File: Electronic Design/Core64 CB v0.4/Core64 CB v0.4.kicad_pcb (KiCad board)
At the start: 2 copper layers, 85 x 85 mm, 36 parts, among them J1 TSM-116-03-T-SV‎, J2 TSM-116-03-T-SV‎, U10 TS3A4751PWR, U11 TS3A4751PWR, U5 SI7210-B-01, U6 SI7210-B-02, U7 SI7210-B-03, U8 SI7210-B-04, U9 LTR-329ALS-01, X1 SFH11-NBPC-D03-ST-BK

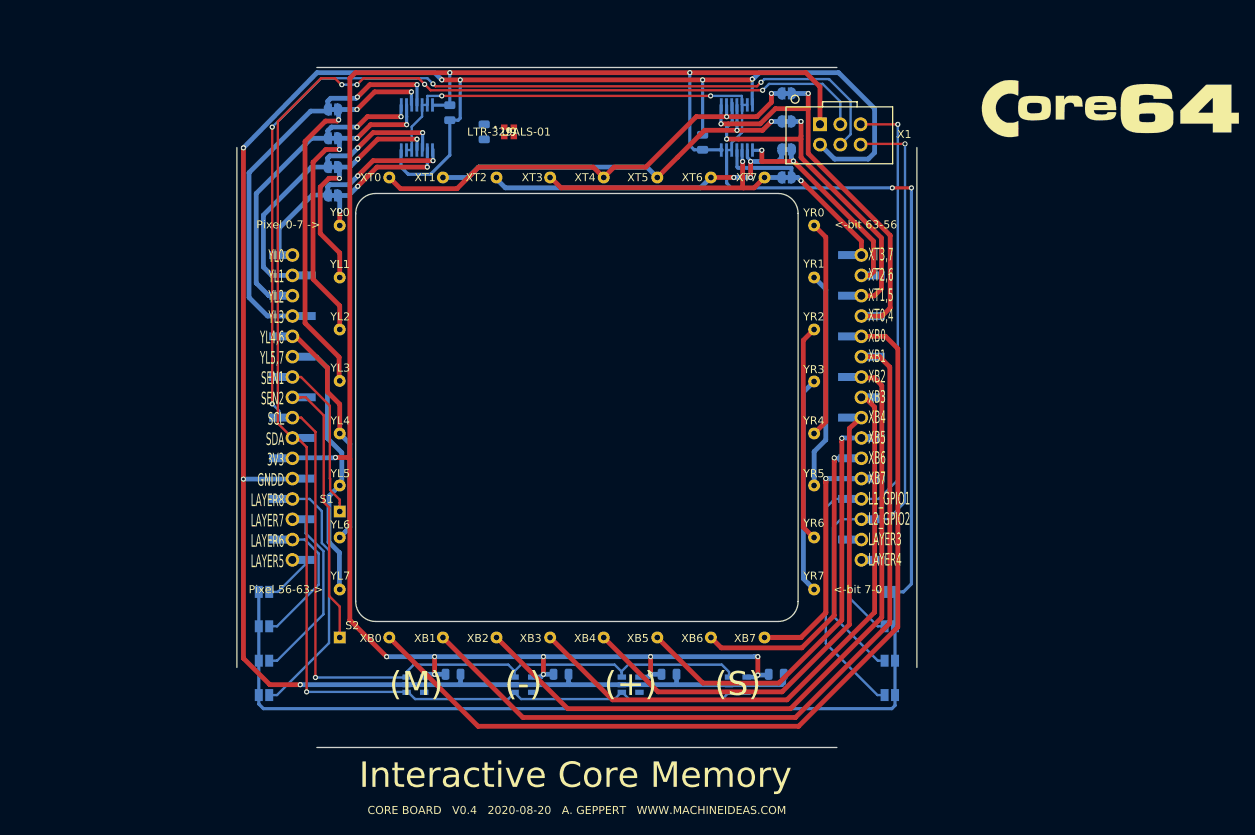
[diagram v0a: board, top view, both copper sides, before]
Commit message: Complete draft of Core Board with updated Core64 Logo
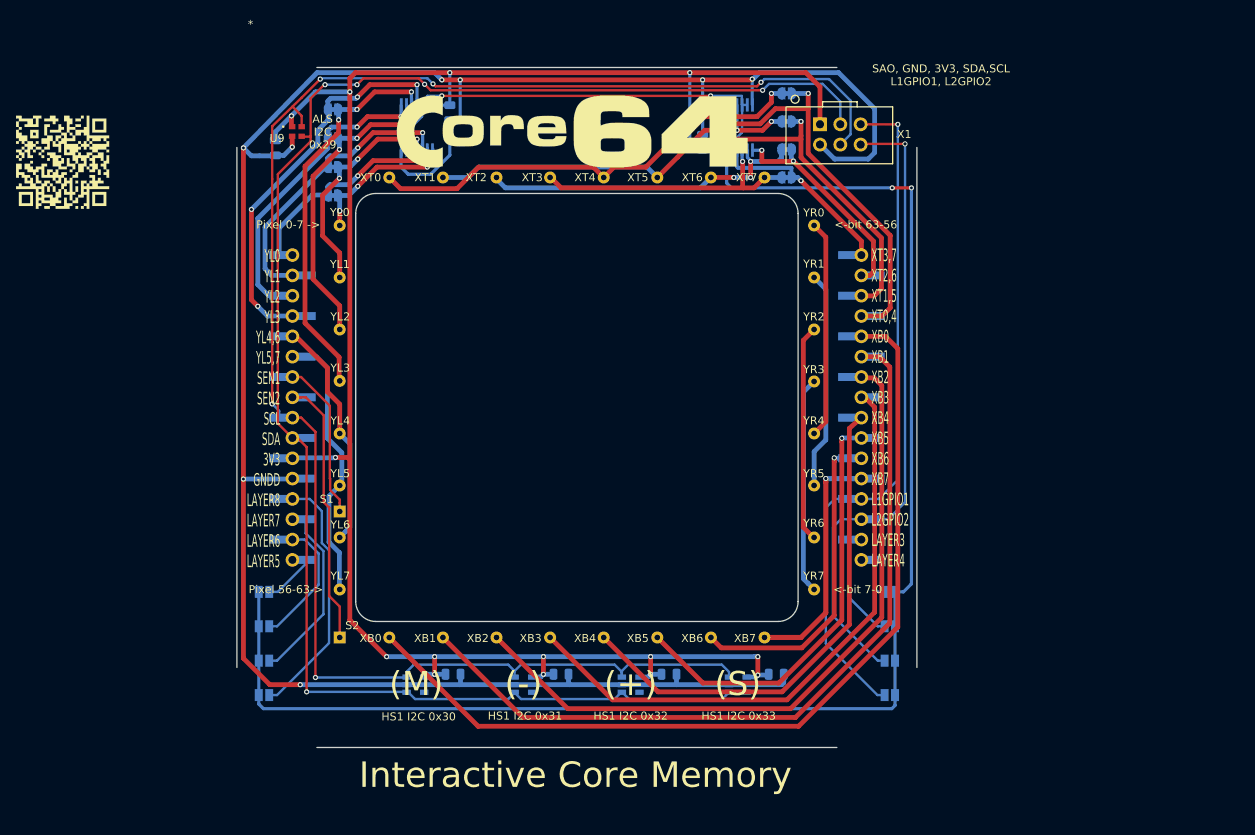
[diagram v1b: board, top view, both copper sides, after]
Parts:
- removed the L2 at (66.9, -37.0)
- added L1: Core_64_Logo_9mm_tall, Core_Memory_8x8_Array:Core64_Logo_9mm_tall, F.Cu at (0.00, -34.5)
- L2: renamed from L1; moved to F.Cu
- moved U9 26.5 mm to (-35.0, -34.5)
- moved C13 26.2 mm to (-37.7, -32.5)
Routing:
- net 3V3_800mA: track 233.9 -> 247.7 mm, vias 12 -> 14
- net GNDD: track 274.7 -> 283.0 mm, vias 7 -> 8
- net I2C_CLOCK: track 212.7 -> 215.7 mm
- net H_YL3: track 52.6 -> 51.1 mm, vias 2 -> 4
- net H_YL2: track 40.4 -> 39.1 mm
- net H_YL1: track 39.4 -> 38.2 mm
- net YL1: track 29.6 -> 28.6 mm
- net YL2: track 39.5 -> 38.5 mm
- net YL3: track 49.9 -> 49.0 mm
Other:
- board text added: "ALS I2C 0x29"
- board text added: "HS1 I2C 0x30"
- board text added: "HS1 I2C 0x31"
- board text added: "HS1 I2C 0x32"
- board text added: "HS1 I2C 0x33"
- board text added: "SAO, GND, 3V3, SDA,SCL L1GPIO1, L2GPIO2"
- board text added: "XT3,7 XT2,6 XT1,5 XT0,4 XB0 XB1 XB2 XB3 XB4 XB5 XB6 XB7 L1GPIO1 L2GPIO2 LAYER3 LAYER4"
- board text removed: "XT3,7 XT2,6 XT1,5 XT0,4 XB0 XB1 XB2 XB3 XB4 XB5 XB6 XB7 L1_GPIO1 L2_GPIO2 LAYER3 LAYER4"

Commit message: Update Core 64 logo
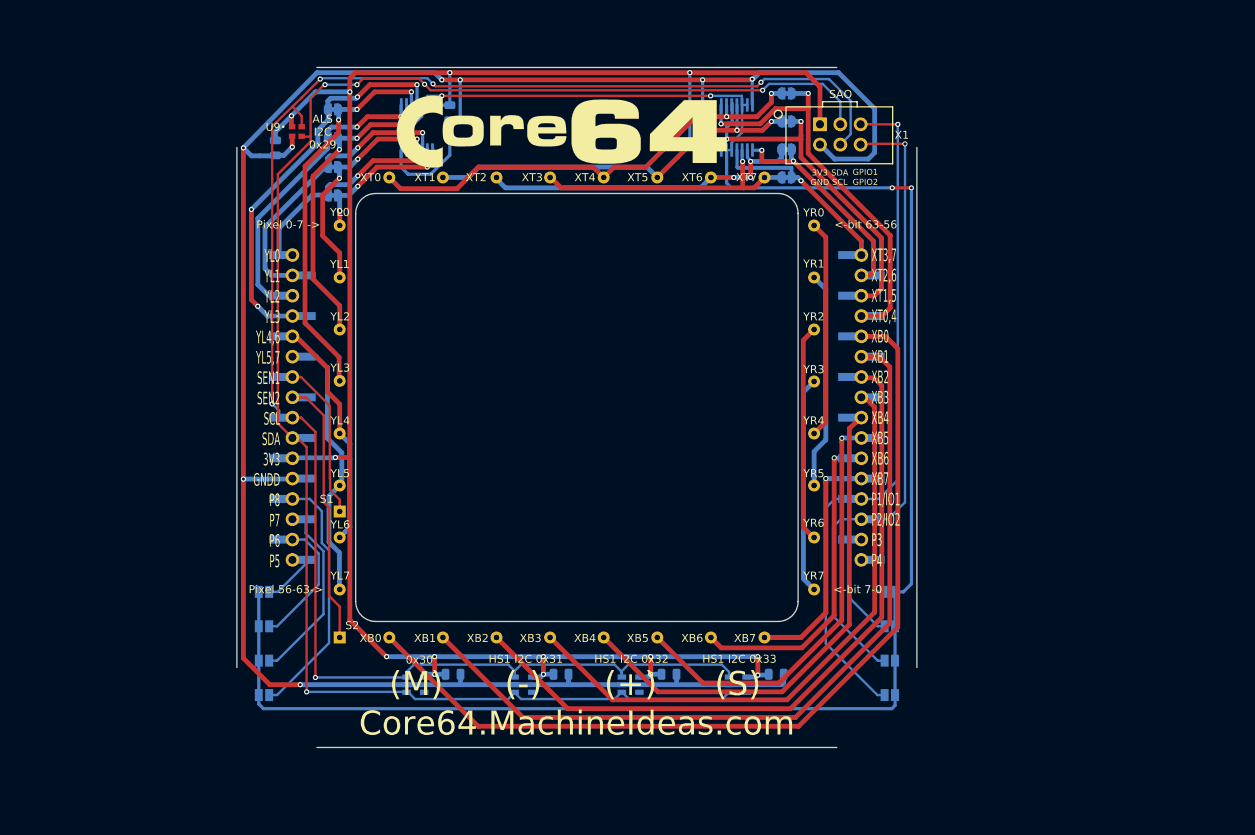
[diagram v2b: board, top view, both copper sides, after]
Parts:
- removed L2: Core_64_Github_Link, Core_Memory_8x8_Array:Github_Link
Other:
- board text added: "0x30"
- board text added: "CORE BOARD V0.4 2020-08-21 ANDY GEPPERT CORE64.MACHINEIDEAS.COM"
- board text added: "Core64.MachineIdeas.com"
- board text added: "XT3,7 XT2,6 XT1,5 XT0,4 XB0 XB1 XB2 XB3 XB4 XB5 XB6 XB7 P1/IO1 P2/IO2 P3 P4"
- board text added: "YL0 YL1 YL2 YL3 YL4,6 YL5,7 SEN1 SEN2 SCL SDA 3V3 GNDD P8 P7 P6 P5"
- board text removed: "CORE BOARD V0.3 2020-04-17 A. GEPPERT WWW.MACHINEIDEAS.COM"
- board text removed: "CORE BOARD V0.4 2020-08-20 A. GEPPERT WWW.MACHINEIDEAS.COM"
- board text removed: "HS1 I2C 0x30"
- board text removed: "SAO, GND, 3V3, SDA,SCL L1GPIO1, L2GPIO2"
- board text removed: "XT3,7 XT2,6 XT1,5 XT0,4 XB0 XB1 XB2 XB3 XB4 XB5 XB6 XB7 +VSW SIG1 GND GPIO2"
- board text removed: "XT3,7 XT2,6 XT1,5 XT0,4 XB0 XB1 XB2 XB3 XB4 XB5 XB6 XB7 L1GPIO1 L2GPIO2 LAYER3 LAYER4"
- board text removed: "YL0 YL1 YL2 YL3 YL4,6 YL5,7 SEN1 SEN2 CLK DAT 3V3 GNDD HALL1 HALL2 HALL3 HALL4"
- board text removed: "YL0 YL1 YL2 YL3 YL4,6 YL5,7 SEN1 SEN2 SCL SDA 3V3 GNDD LAYER8 LAYER7 LAYER6 LAYER5"

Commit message: Add Mode - + Set button in Commodore font, clean-up silk screen, solder mask between 16x T.H. and pads
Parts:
- added L2: Core_64_M-+S_Buttons_4mm, Core_Memory_8x8_Array:Core64-M_-_+_S_Buttons, F.Cu at (-0.98, 34.6)
- moved L1 1.83 mm to (1.81, -34.8)
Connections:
- net LAYER_1 renamed PLANE_1
- net LAYER_2 renamed PLANE_2
- net LAYER_3 renamed PLANE_3
- net LAYER_4 renamed PLANE_4
- net LAYER_5 renamed PLANE_5
- net LAYER_6 renamed PLANE_6
- net LAYER_7 renamed PLANE_7
- net LAYER_8 renamed PLANE_8
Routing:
- net PLANE_7: track 23.8 -> 26.1 mm
- net PLANE_8: track 33.0 -> 35.0 mm
- net PLANE_4: track 6.62 -> 8.62 mm
- net PLANE_3: track 14.9 -> 16.9 mm
- net PLANE_2: track 82.2 -> 84.2 mm
- net PLANE_1: track 86.5 -> 88.5 mm
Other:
- board text added: "0x31"
- board text added: "0x32"
- board text added: "0x33"
- board text added: "ALS 0x29"
- board text added: "CORE BOARD V0.4 2020-08-21 ANDY GEPPERT"
- board text added: "Pixel 0-7->"
- board text removed: "(+)"
- board text removed: "(-)"
- board text removed: "(M)"
- board text removed: "(S)"
- board text removed: "ALS I2C 0x29"
- board text removed: "CORE BOARD V0.4 2020-08-21 ANDY GEPPERT CORE64.MACHINEIDEAS.COM"
- board text removed: "HS1 I2C 0x31"
- board text removed: "HS1 I2C 0x32"
- board text removed: "HS1 I2C 0x33"
- board text removed: "Pixel 0-7 ->"

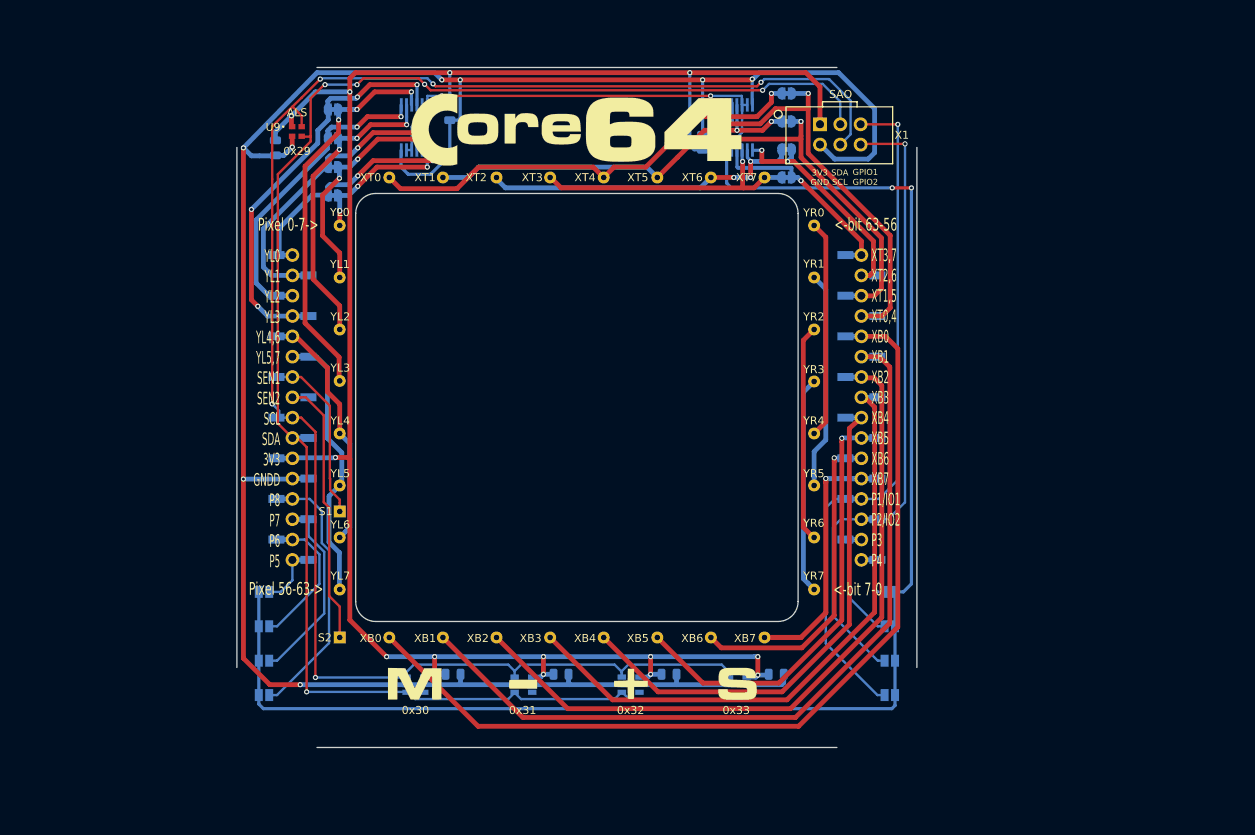
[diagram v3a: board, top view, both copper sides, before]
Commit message: CB V0.4 as prototype and BOM parts ordered
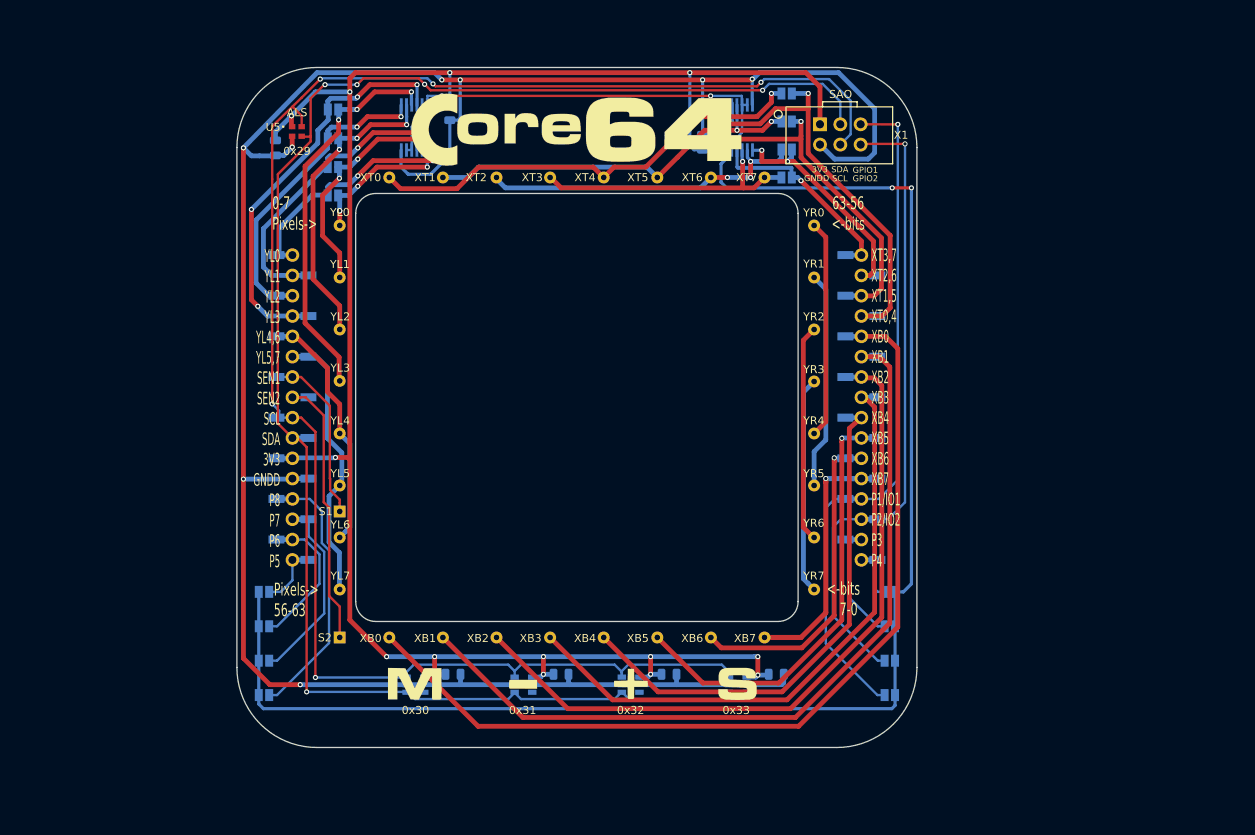
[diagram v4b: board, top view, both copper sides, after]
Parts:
- JP1, JP2, JP3, JP4, JP5, JP6, JP7, JP8: footprint Jumper:SolderJumper-2_P1.3mm_Bridged_RoundedPad1.0x1.5mm -> Jumper:SolderJumper-2_P1.3mm_Open_Pad1.0x1.5mm
- renumbered C9 to C1, C10 to C2, C11 to C3, C12 to C4, C13 to C5, C1 to C6, C2 to C7, U5 to U1, U6 to U2, U7 to U3, U8 to U4, U9 to U5, U10 to U6, U11 to U7
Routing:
- net ENABLE: track 244.1 -> 245.0 mm
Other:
- board text added: "0-7 Pixels->"
- board text added: "63-56 <-bits"
- board text added: "<-bits 7-0"
- board text added: "CORE BOARD V0.4 2020-08-22 ANDY GEPPERT"
- board text added: "IO1 IO2"
- board text added: "Pixels-> 56-63"
- board text added: "XT3,7 XT2,6 XT1,5 XT0,4 XB0 XB1 XB2 XB3 XB4 XB5 XB6 XB7 P1 P2 P3 P4"
- board text removed: "<-bit 63-56"
- board text removed: "<-bit 7-0"
- board text removed: "CORE BOARD V0.4 2020-08-21 ANDY GEPPERT"
- board text removed: "Pixel 0-7->"
- board text removed: "Pixel 56-63->"

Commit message: Update Simple Add Ons #2 on all schematics PCBs
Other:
- board text added: "SAO#2"
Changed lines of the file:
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@@
   (general
     (thickness 1.6)
-    (drawings 42)
+    (drawings 43)
     (tracks 706)
     (zones 0)
@@
       (effects (font (size 1 1) (thickness 0.15)))
     )
-    (fp_text user SAO (at 0.1 -5) (layer F.SilkS)
+    (fp_text user SAO#2 (at 0.1 -5) (layer F.SilkS)
       (effects (font (size 1 1) (thickness 0.15)))
     )
@@
       (net 35 H_XT3-7))
   )
+  (gr_text SAO#2 (at 33.015 -39.15) (layer B.SilkS)
+    (effects (font (size 1 1) (thickness 0.15)) (justify mirror))
+  )
   (gr_text "IO1\nIO2\n" (at 30.115 12.75) (layer B.SilkS)
